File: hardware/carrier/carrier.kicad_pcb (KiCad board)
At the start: 4 copper layers, 164.9 x 102 mm, 171 parts, among them J1 Harness_4Runner, J2 Pi 4 GPIO, J3 UART, J4 MIC, M1 FAN1, M2 FAN2, Q1 BUK7Y4R8-60E, Q2 BUK7Y4R8-60E, Q3 MMBT3904, Q4 MMBT3904, Q5 MMBT3904, Q6 2N7002, Q7 2N7002, U1 LM74800-Q1, U2 ADS1115IDGS, U3 DS3231SN, U4 CAT24C32, U5 LM61460-Q1, U6 TLV75533PDBV, U7 TAS6424E-Q1, U8 PCM1808-Q1, X1 12.288MHz

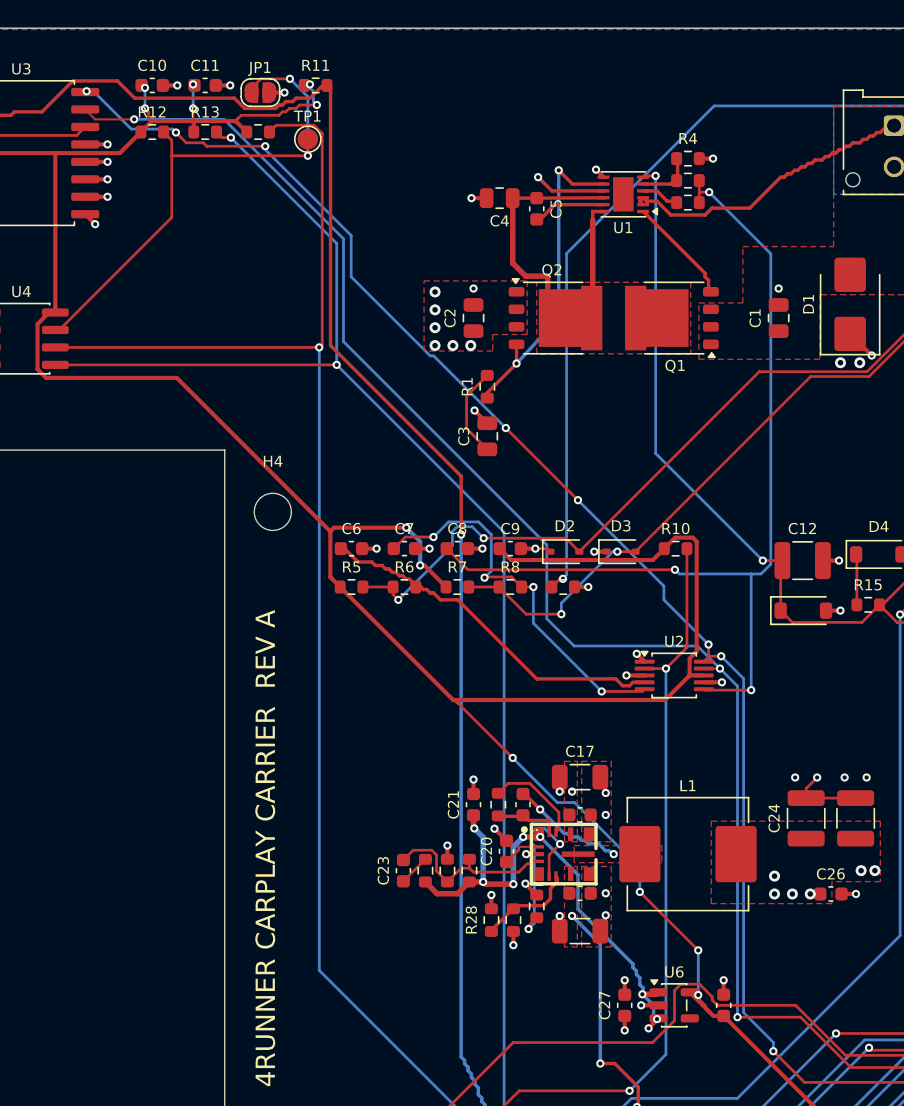
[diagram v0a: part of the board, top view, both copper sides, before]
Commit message: Carrier: via-off-pad tool, PCBWay assembly files, layout and verification updates
Adds the PCBWay BOM/CPL/assembly drawings, the via_off_pad.py cleanup tool,
and a small ERC test schematic. Updates the board, gerbers, build script,
maze router and VERIFICATION.md. Adds the project KiCad agent skills.

Co-Authored-By: Claude Sonnet 5.5 <noreply@anthropic.com>
Claude-Session: https://claude.ai/code/session_01TspzXdhsWVb3sDXDg4j43E
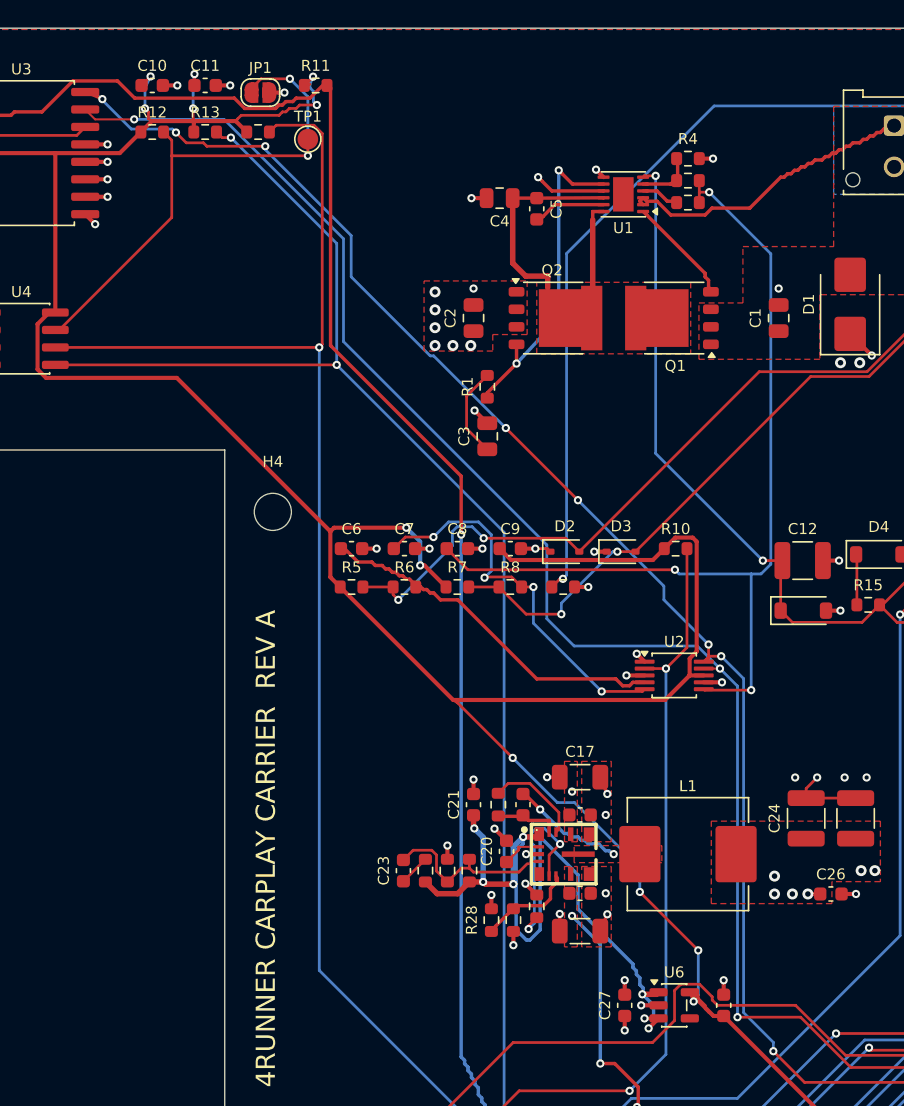
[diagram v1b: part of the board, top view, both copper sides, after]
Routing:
- net +5V: track 45.0 -> 65.2 mm, vias 21 -> 20
- net +3V3: track 427.2 -> 433.4 mm
- net GND: track 145.0 -> 147.6 mm
- net /I2C_SCL: track 163.1 -> 165.7 mm
- net +12V_PROT: track 80.3 -> 82.5 mm
